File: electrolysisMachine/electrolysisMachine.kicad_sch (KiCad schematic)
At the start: 25 parts

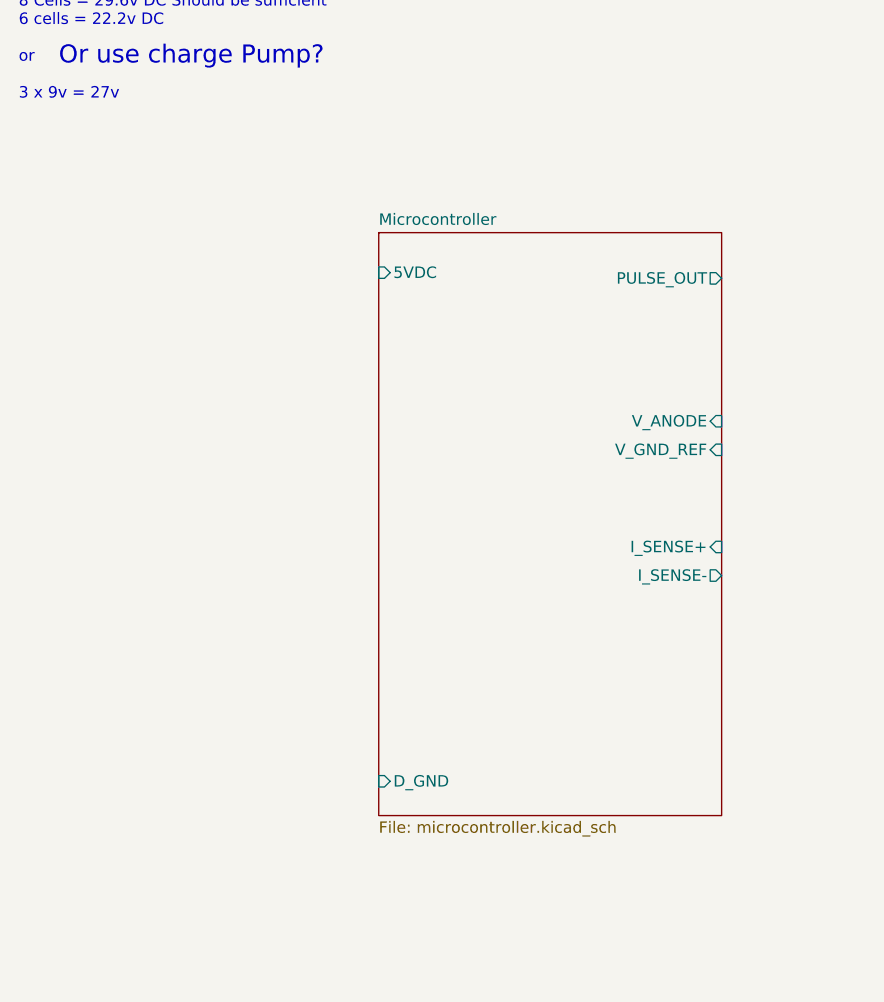
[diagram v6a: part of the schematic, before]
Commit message: Added test circuit schematic
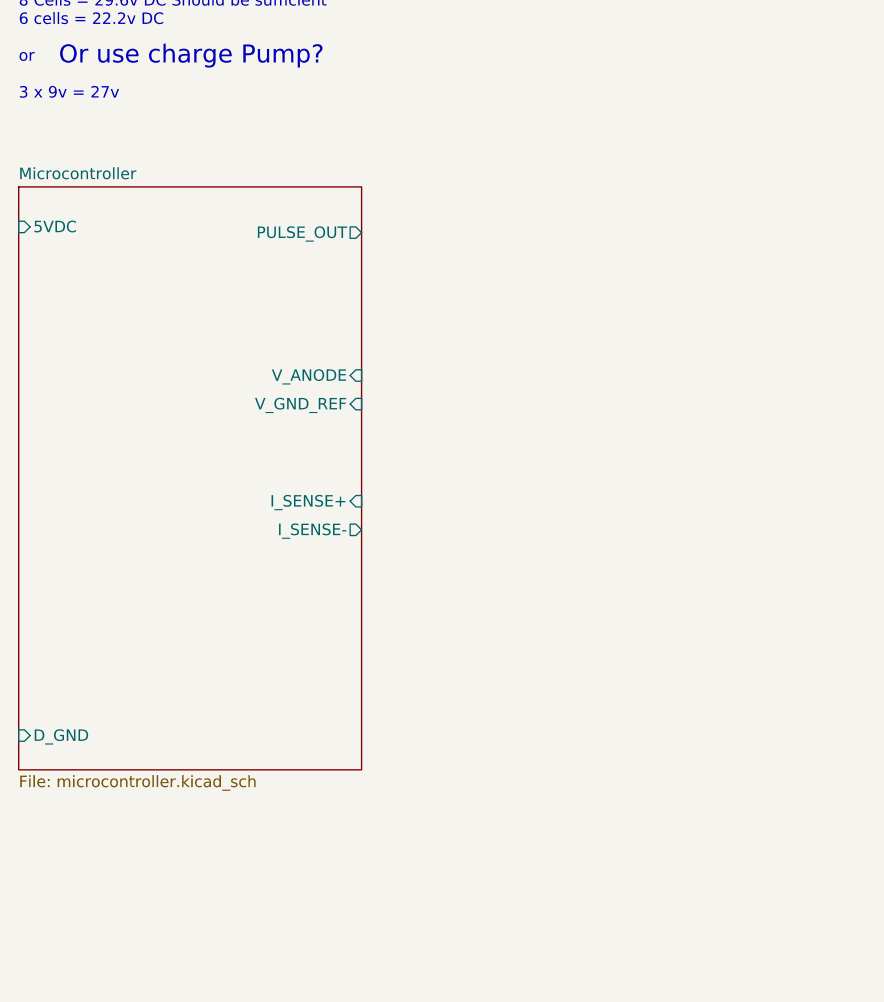
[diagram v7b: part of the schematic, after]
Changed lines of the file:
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@@
     (pin "2")
   )
-  (sheet (at 54.61 95.25) (size 38.1 64.77) (fields_autoplaced)
+  (sheet (at 14.605 90.17) (size 38.1 64.77) (fields_autoplaced)
     (stroke (width 0.1524) (type solid) (color 0 0 0 0))
     (fill (color 56 255 251 0.3400))
-    (property "Sheet name" "Microcontroller" (id 0) (at 54.61 94.5384 0)
+    (property "Sheet name" "Microcontroller" (id 0) (at 14.605 89.4584 0)
       (effects (font (size 1.27 1.27)) (justify left bottom))
     )
-    (property "Sheet file" "microcontroller.kicad_sch" (id 1) (at 54.61 160.6046 0)
+    (property "Sheet file" "microcontroller.kicad_sch" (id 1) (at 14.605 155.5246 0)
       (effects (font (size 1.27 1.27)) (justify left top))
     )
-    (pin "5VDC" input (at 54.61 99.695 180)
+    (pin "5VDC" input (at 14.605 94.615 180)
       (effects (font (size 1.27 1.27)) (justify left))
     )
-    (pin "D_GND" input (at 54.61 156.21 180)
+    (pin "D_GND" input (at 14.605 151.13 180)
       (effects (font (size 1.27 1.27)) (justify left))
     )
-    (pin "PULSE_OUT" output (at 92.71 100.33 0)
+    (pin "PULSE_OUT" output (at 52.705 95.25 0)
       (effects (font (size 1.27 1.27)) (justify right))
     )
-    (pin "V_GND_REF" input (at 92.71 119.38 0)
+    (pin "V_GND_REF" input (at 52.705 114.3 0)
       (effects (font (size 1.27 1.27)) (justify right))
     )
-    (pin "V_ANODE" input (at 92.71 116.205 0)
+    (pin "V_ANODE" input (at 52.705 111.125 0)
       (effects (font (size 1.27 1.27)) (justify right))
     )
-    (pin "I_SENSE+" input (at 92.71 130.175 0)
+    (pin "I_SENSE+" input (at 52.705 125.095 0)
       (effects (font (size 1.27 1.27)) (justify right))
     )
-    (pin "I_SENSE-" output (at 92.71 133.35 0)
+    (pin "I_SENSE-" output (at 52.705 128.27 0)
       (effects (font (size 1.27 1.27)) (justify right))
     )
@@
       (reference "C?") (unit 1) (value "100n") (footprint "Capacitor_SMD:C_0805_2012Metric_Pad1.18x1.45mm_HandSolder")
     )
+    (path "/40e57fa2-6889-463a-9517-9491e4c77d28/008d8cb8-35a0-4fae-a09f-14ae3642e3c2"
+      (reference "D?") (unit 1) (value "BZV55B18") (footprint "Diode_SMD:D_MiniMELF")
+    )
     (path "/580159ba-edd3-41e3-abcd-ff933f8f1a26/537fd7c3-c519-4423-a53d-bdc19ad347f4"
       (reference "D?") (unit 1) (value "LED_BLUE") (footprint "Diode_SMD:D_0805_2012Metric_Pad1.15x1.40mm_HandSolder")
@@
     (path "/9b6bf923-eedb-44ae-a758-7ce1f7749c86"
       (reference "D?") (unit 1) (value "LED_ORANGE") (footprint "Diode_SMD:D_0805_2012Metric_Pad1.15x1.40mm_HandSolder")
+    )
+    (path "/40e57fa2-6889-463a-9517-9491e4c77d28/b3d899dc-a9f7-4753-8390-745856ca9a17"
+      (reference "D?") (unit 1) (value "BZV55B4V7") (footprint "Diode_SMD:D_MiniMELF")
     )
     (path "/580159ba-edd3-41e3-abcd-ff933f8f1a26/899e3c83-3f2c-47e5-bc11-4e72c829a579"
@@
       (reference "PT?") (unit 1) (value "5k") (footprint "Potentiometer_THT:Potentiometer_Alpha_RD901F-40-00D_Single_Vertical_CircularHoles")
     )
+    (path "/40e57fa2-6889-463a-9517-9491e4c77d28/d1c434bf-b7f0-418c-819d-86a4a535331b"
+      (reference "PT?") (unit 1) (value "250k") (footprint "Potentiometer_THT:Potentiometer_Alpha_RD901F-40-00D_Single_Vertical_CircularHoles")
+    )
     (path "/e0cbe4a3-1a68-4ab3-9225-2bed0a0a2a30"
       (reference "PT?") (unit 1) (value "5k") (footprint "Potentiometer_THT:Potentiometer_Alpha_RD901F-40-00D_Single_Vertical_CircularHoles")
@@
     (path "/d5711a27-fee6-44ac-9c40-ee5460af8403"
       (reference "Q?") (unit 1) (value "2N3906") (footprint "Package_TO_SOT_THT:TO-92_Inline")
+    )
+    (path "/40e57fa2-6889-463a-9517-9491e4c77d28/0f80cb95-ecb5-4470-913b-3cb7006e6cd7"
+      (reference "R?") (unit 1) (value "100r") (footprint "Resistor_SMD:R_0805_2012Metric_Pad1.20x1.40mm_HandSolder")
     )
     (path "/24f49b90-6628-42fc-8dff-fc75e215619a"
@@
       (reference "R?") (unit 1) (value "2k9") (footprint "Resistor_SMD:R_0805_2012Metric_Pad1.20x1.40mm_HandSolder")
     )
+    (path "/40e57fa2-6889-463a-9517-9491e4c77d28/3ed0041b-48be-427d-8cdf-667405c53983"
+      (reference "R?") (unit 1) (value "470r") (footprint "Resistor_SMD:R_0805_2012Metric_Pad1.20x1.40mm_HandSolder")
+    )
+    (path "/40e57fa2-6889-463a-9517-9491e4c77d28/5788ce6d-136b-45ae-a490-5ae9d055d0d7"
+      (reference "R?") (unit 1) (value "100r") (footprint "Resistor_SMD:R_0805_2012Metric_Pad1.20x1.40mm_HandSolder")
+    )
     (path "/5a1f5af1-0c2f-4743-a78b-6b82fe4d0049"
       (reference "R?") (unit 1) (value "15k") (footprint "Resistor_SMD:R_0805_2012Metric_Pad1.20x1.40mm_HandSolder")
@@
     (path "/63487d49-6c2a-4ab5-a78f-fbf4d69ef393"
       (reference "R?") (unit 1) (value "1k") (footprint "Resistor_SMD:R_0805_2012Metric_Pad1.20x1.40mm_HandSolder")
+    )
+    (path "/40e57fa2-6889-463a-9517-9491e4c77d28/82303ec7-9d50-435b-ac52-53267ca75f47"
+      (reference "R?") (unit 1) (value "10k") (footprint "Resistor_SMD:R_0805_2012Metric_Pad1.20x1.40mm_HandSolder")
+    )
+    (path "/40e57fa2-6889-463a-9517-9491e4c77d28/952489a4-27d5-4ffa-9398-f00028963d4d"
+      (reference "R?") (unit 1) (value "33k") (footprint "Resistor_SMD:R_0805_2012Metric_Pad1.20x1.40mm_HandSolder")
     )
     (path "/af21d486-1a1b-4048-b393-7e467d3ec161"
@@
       (reference "R?") (unit 1) (value "2k2") (footprint "Resistor_SMD:R_0805_2012Metric_Pad1.20x1.40mm_HandSolder")
     )
+    (path "/40e57fa2-6889-463a-9517-9491e4c77d28/c04bf0ef-a21a-496c-abc8-f1cc3fd599a8"
+      (reference "R?") (unit 1) (value "10k") (footprint "Resistor_SMD:R_0805_2012Metric_Pad1.20x1.40mm_HandSolder")
+    )
     (path "/580159ba-edd3-41e3-abcd-ff933f8f1a26/e5d9fe17-9394-4948-b170-6d91b739fa5d"
